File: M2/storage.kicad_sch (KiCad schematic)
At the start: 11 parts, among them IC1 XT25F128FWOIGT-W, J1 Micro_SD_Card_Det2

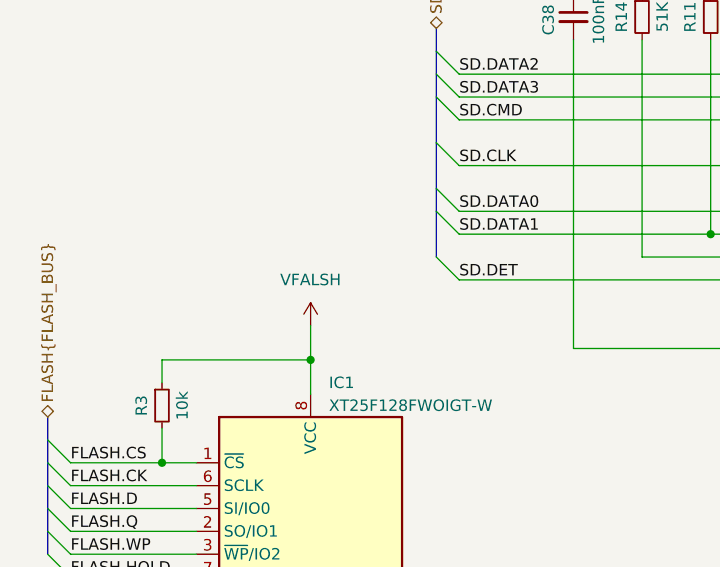
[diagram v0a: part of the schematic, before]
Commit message: Fix typo in schematic for FLASH
Correction on schematic from FALSH to FLASH. Simple typo correction, nothing more.
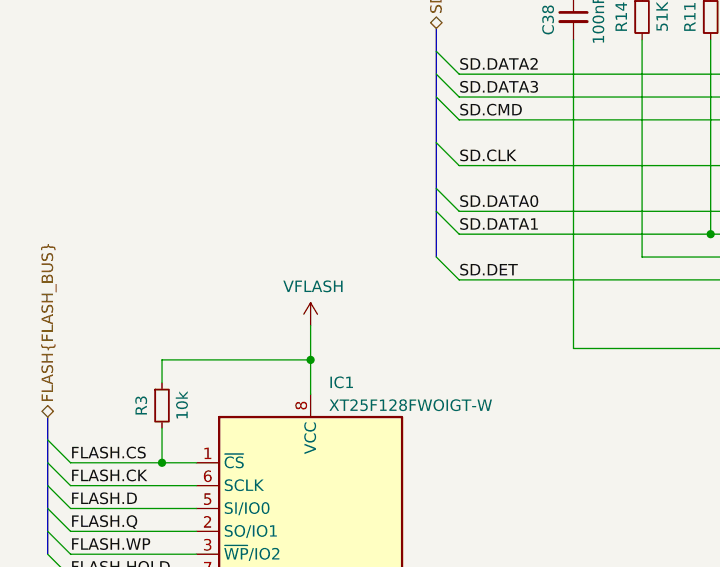
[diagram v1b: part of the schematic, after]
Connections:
- net VFALSH renamed VFLASH
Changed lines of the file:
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@@
 		(on_board yes)
 		(dnp no)
-		(fields_autoplaced yes)
 		(property "Reference" "#PWR033"
 			(at 54.61 76.2 0)
@@
 			)
 		)
-		(property "Value" "VFALSH"
-			(at 54.61 67.31 0)
+		(property "Value" "VFLASH"
+			(at 51.562 68.072 0)
 			(effects
 				(font
 					(size 1.27 1.27)
 				)
+				(justify left)
 			)
 		)
